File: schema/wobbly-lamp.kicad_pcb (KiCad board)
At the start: 2 copper layers, 70 x 50 mm, 33 parts, among them IC1 ATMEGA8-AI, Q1 IRLML0030TRPbF, Q2 IRLML0030TRPbF, Q3 IRLML0030TRPbF, U1 LD1117S33TR

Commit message: Redraw PCB
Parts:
- moved PWR1 55.9 mm to (74.5, 27.0), turned to 270 degrees
- moved C1 47.4 mm to (70.5, 18.0), turned to 90 degrees
- moved R10 44.2 mm to (17.8, 50.8), turned to 90 degrees
- moved JP1 38.9 mm to (23.0, 52.2), turned to 0 degrees
- moved U1 36.2 mm to (61.8, 19.5), turned to 0 degrees
- moved C2 31.3 mm to (55.0, 21.8), turned to 0 degrees
- moved ISP1 28.0 mm to (39.0, 58.4)
- moved L1 22.9 mm to (28.6, 36.0)
- moved PL1 22.8 mm to (25.0, 30.0), turned to 270 degrees
- moved C4 20.5 mm to (29.2, 32.4), turned to 180 degrees
- moved C3 17.7 mm to (31.4, 37.4)
- moved R2 17.4 mm to (26.4, 39.0), turned to 0 degrees
- moved PR1 14.3 mm to (50.0, 30.0), turned to 270 degrees
- moved C5 14.3 mm to (57.2, 29.0), turned to 90 degrees
- moved Q3 13.4 mm to (64.8, 51.5)
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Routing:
- net +12V: track 124.3 -> 31.0 mm
- net +3.3V: track 102.6 -> 162.9 mm, vias 0 -> 2
- net Net-(IC1-Pad9): track 0.03 -> 39.3 mm, vias 0 -> 2
- net RST: track 9.22 -> 44.7 mm, vias 0 -> 2
- net PWM_green: track 5.15 -> 33.7 mm
- net PWM_red: track 11.5 -> 37.4 mm
- net 0g: track 0.00 -> 24.8 mm, vias 0 -> 2
- net SCK: track 0.00 -> 24.1 mm
- net pot1: track 15.8 -> 33.7 mm
- net pot2: track 20.2 -> 28.4 mm
- net MOSI: track 29.9 -> 36.9 mm
- net gS: track 7.98 -> 2.44 mm
- net Net-(PL1-Pad4): track 2.83 -> 8.00 mm
- net Y: track 12.2 -> 9.11 mm
- net MISO: track 18.9 -> 21.7 mm, vias 0 -> 2
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
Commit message: Add missing path
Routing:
- net Net-(IC1-Pad9): track 39.3 -> 43.3 mm

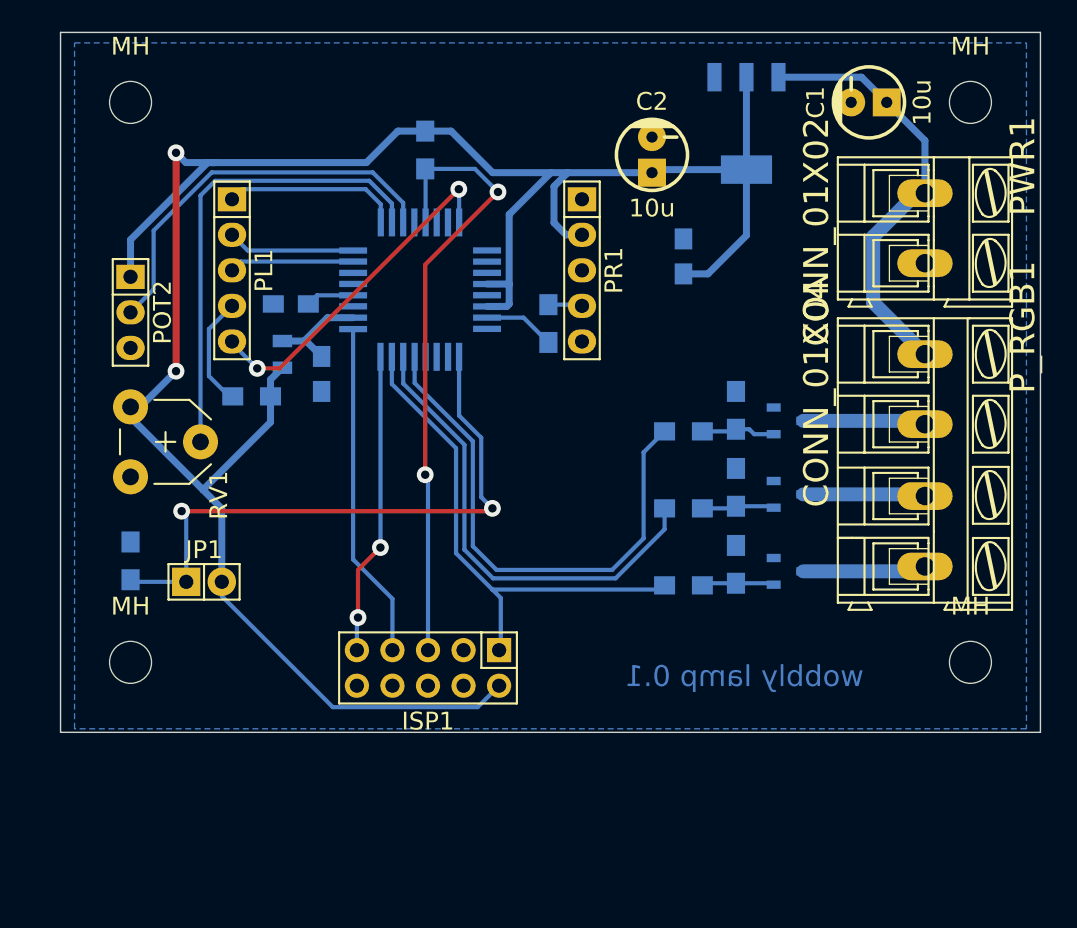
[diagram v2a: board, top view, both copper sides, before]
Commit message: Add first working PCB, tiny version
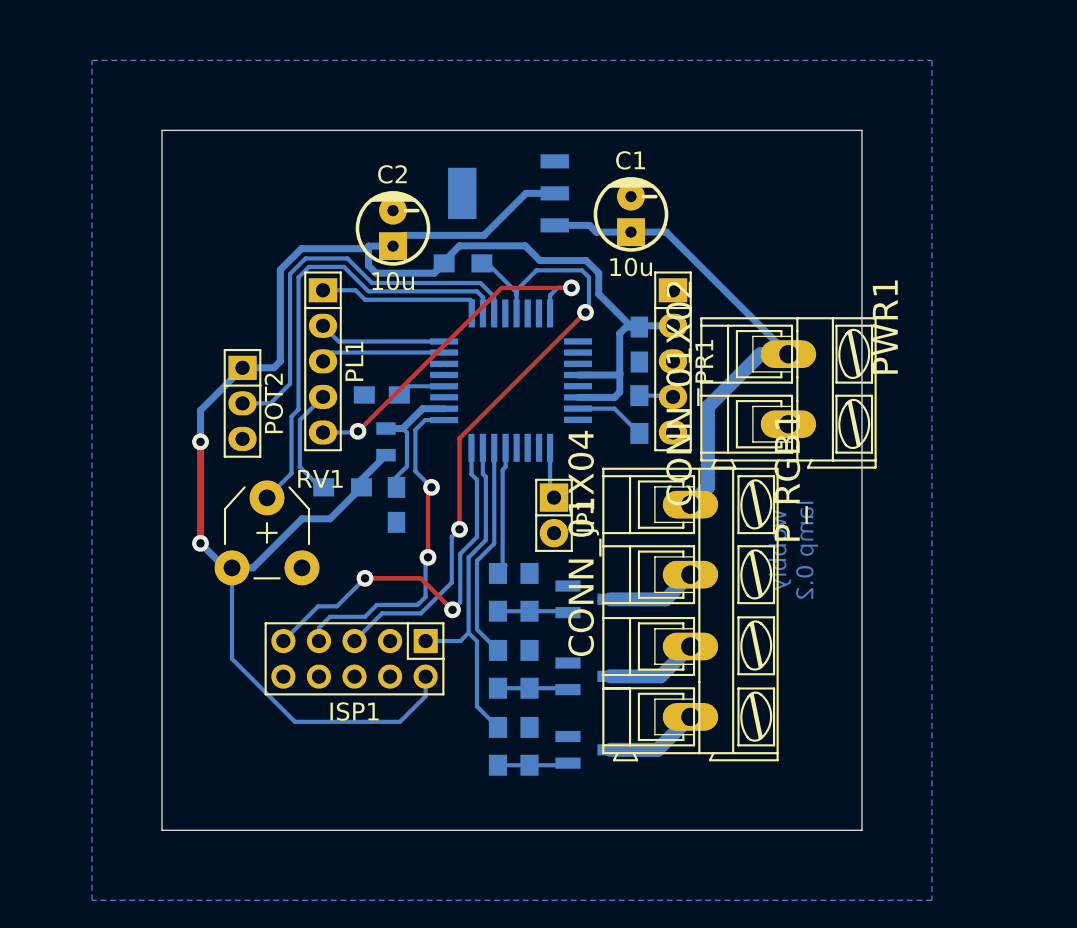
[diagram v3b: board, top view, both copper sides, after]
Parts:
- removed MH (x4): MountingHole_3mm_RevA_Date21Jun2010, Mounting_Holes:MountingHole_3mm
- removed R10: 22k, Resistors_SMD:R_0805_HandSoldering
- Q1, Q2, Q3: footprint Local:sot23 -> Housings_SOT-23_SOT-143_TSOT-6:SOT23_FET_Handsoldering
- RV1: value 22k -> 2k2
- moved JP1 25.4 mm to (48.0, 47.5), turned to 270 degrees
- moved P_RGB1 19.9 mm to (57.8, 49.2)
- moved R6 19.7 mm to (46.2, 53.0)
- moved R7 19.7 mm to (46.2, 58.5)
- moved R8 19.7 mm to (46.2, 64.0)
- moved Q2 19.3 mm to (50.5, 59.0)
- moved C2 19.2 mm to (36.5, 27.0)
- moved Q1 19.1 mm to (50.5, 53.5)
- moved Q3 19.1 mm to (50.5, 64.2)
- moved C1 18.8 mm to (53.5, 26.0), turned to 0 degrees
- moved U1 17.7 mm to (44.8, 24.5), turned to 270 degrees
- moved R3 17.5 mm to (44.0, 53.0), turned to 90 degrees
- moved R4 17.5 mm to (44.0, 58.5), turned to 90 degrees
- moved R5 17.5 mm to (44.0, 64.0), turned to 90 degrees
- moved PWR1 15.1 mm to (64.8, 38.5)
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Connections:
- net MOSI renamed PWM_blue
- JP1 pad 2: +3.3V -> GND
- U1 pad 4: +3.3V -> (no net)
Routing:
- net Net-(IC1-Pad9): track 43.3 -> 3.69 mm, vias 2 -> 0
- net +3.3V: track 162.9 -> 127.0 mm
- net PWM_red: track 37.4 -> 9.97 mm
- net PWM_green: track 33.7 -> 15.6 mm
- net PWM_blue: track 36.9 -> 24.8 mm
- net MISO: track 21.7 -> 27.3 mm
- net +12V: track 31.0 -> 35.3 mm
- net red: track 8.79 -> 6.48 mm
- net blue: track 8.84 -> 6.72 mm
- net green: track 8.74 -> 6.63 mm
- net Net-(C3-Pad1): track 7.59 -> 9.37 mm
- net pot1: track 33.7 -> 32.2 mm
- net 0g: track 24.8 -> 25.8 mm
- net RST: track 44.7 -> 45.7 mm
- net X: track 12.7 -> 11.8 mm
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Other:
- board size 70 x 50 mm -> 50 x 50 mm
- board text added: "wobbly lamp 0.2"
- board text removed: "wobbly lamp 0.1"
